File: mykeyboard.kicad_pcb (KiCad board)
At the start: 2 copper layers, 91.4 x 55.9 mm, 23 parts, among them J1 MJ-4PP-9, SW1 SW_PUSH, SW2 SW_PUSH, SW3 SW_PUSH, SW4 SW_PUSH, SW5 SW_PUSH, SW6 SW_PUSH, SW7 SW_PUSH, SW8 SW_PUSH, SW9 SW_PUSH, U1 ProMicro

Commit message: Pro micro の配置と回路の配線
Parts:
- added U1: ProMicro, Keebio-Parts:ArduinoProMicro-BackSide, B.Cu at (137.2, 90.2)
- U1: footprint kbd:ProMicro_v2 -> Keebio-Parts:ArduinoProMicro-BackSide
- moved J1 36.8 mm to (172.7, 75.0)
- moved U1 19.7 mm to (156.2, 90.2)
- moved D1 12.7 mm to (118.1, 104.1), turned to 180 degrees
- moved D5 1.27 mm to (118.1, 108.0)
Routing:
- net row1: track 0.00 -> 113.4 mm
- net col2: track 0.00 -> 95.8 mm
- net col3: track 0.00 -> 93.4 mm
- net row0: track 0.00 -> 87.6 mm
- net GND: track 0.00 -> 71.1 mm
- net col0: track 0.00 -> 58.6 mm
- net VCC: track 0.00 -> 48.7 mm
- net col1: track 0.00 -> 47.4 mm
- net reset: track 0.00 -> 44.7 mm
- net Net-(U1-Pad16): track 0.00 -> 37.1 mm
- net Net-(D2-Pad1): track 0.00 -> 37.1 mm
- net Net-(U1-Pad14): track 0.00 -> 35.3 mm
- net Net-(U1-Pad15): track 0.00 -> 35.3 mm
- net Net-(U1-Pad24): track 0.00 -> 35.3 mm
- net Net-(U1-Pad13): track 0.00 -> 35.3 mm
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
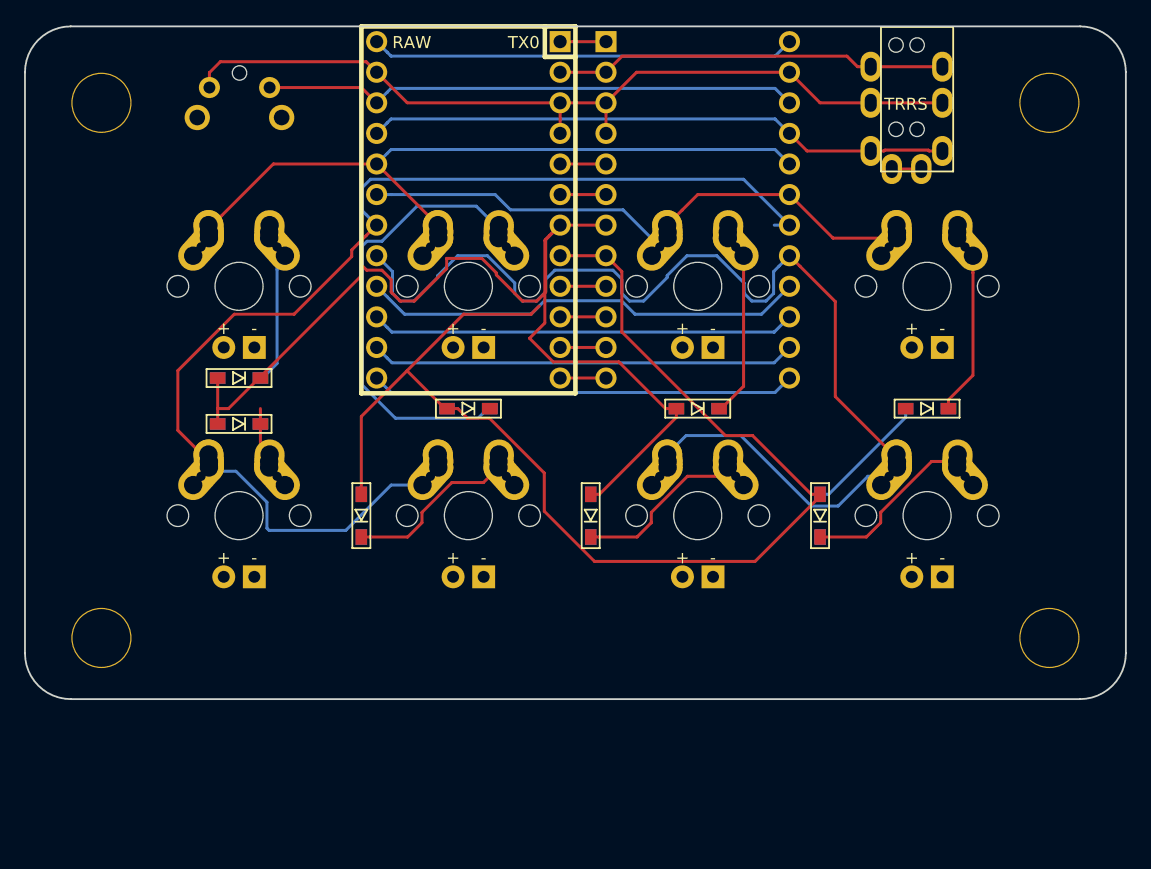
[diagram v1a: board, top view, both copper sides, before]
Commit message: 配線をリセット、ダイオードの位置をまとめた
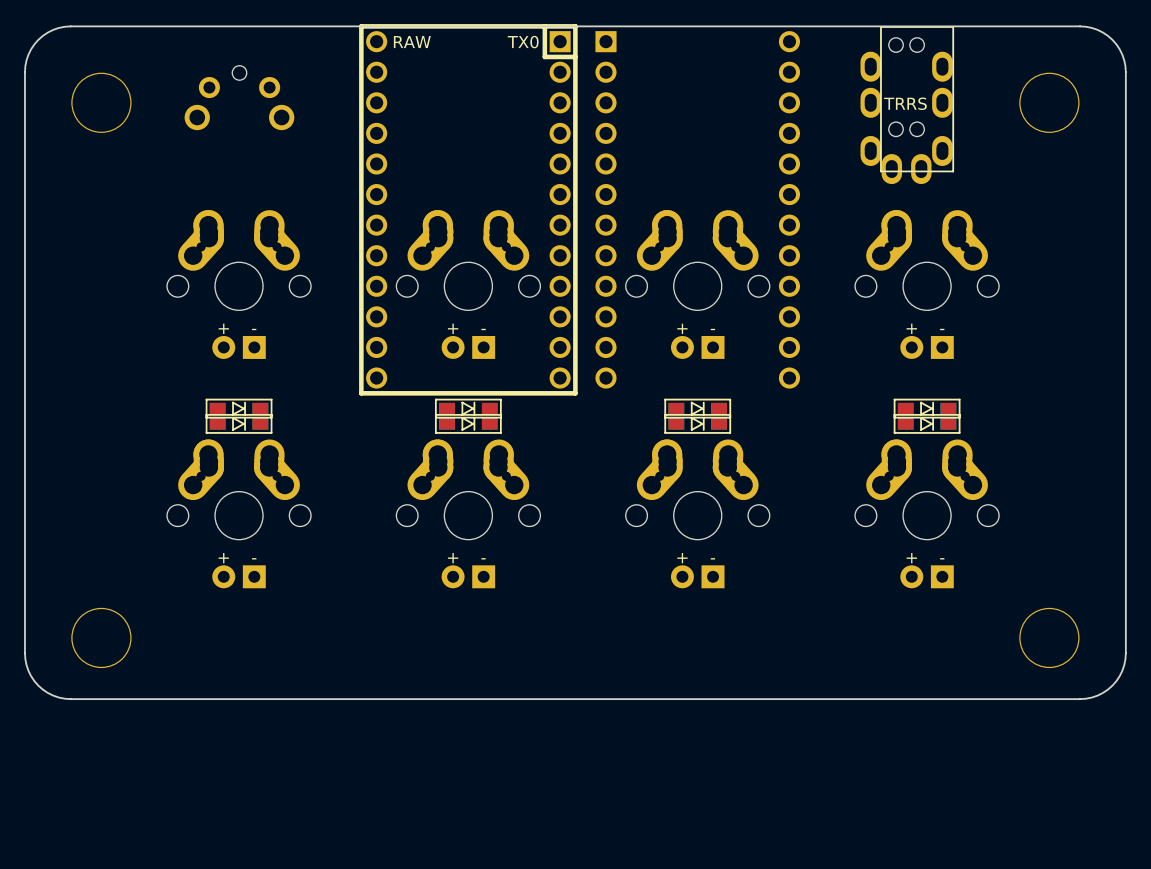
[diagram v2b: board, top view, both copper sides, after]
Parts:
- moved D7 11.7 mm to (156.2, 108.0), turned to 180 degrees
- moved D6 11.7 mm to (137.2, 108.0), turned to 180 degrees
- moved D8 11.7 mm to (175.3, 108.0), turned to 180 degrees
- moved D1 2.54 mm to (118.1, 106.7)
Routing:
- net row1: track 113.4 -> 0.00 mm
- net col2: track 95.8 -> 0.00 mm
- net col3: track 93.4 -> 0.00 mm
- net row0: track 87.6 -> 0.00 mm
- net GND: track 71.1 -> 0.00 mm
- net col0: track 58.6 -> 0.00 mm
- net VCC: track 48.7 -> 0.00 mm
- net col1: track 47.4 -> 0.00 mm
- net reset: track 44.7 -> 0.00 mm
- net Net-(U1-Pad16): track 37.1 -> 0.00 mm
- net Net-(D2-Pad1): track 37.1 -> 0.00 mm
- net Net-(U1-Pad14): track 35.3 -> 0.00 mm
- net Net-(U1-Pad15): track 35.3 -> 0.00 mm
- net Net-(U1-Pad24): track 35.3 -> 0.00 mm
- net Net-(U1-Pad13): track 35.3 -> 0.00 mm
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
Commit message: 回路図の Pro Micro のフットプリントを Keebio の Backside 版に更新、PCB にフットプリントを全て反映
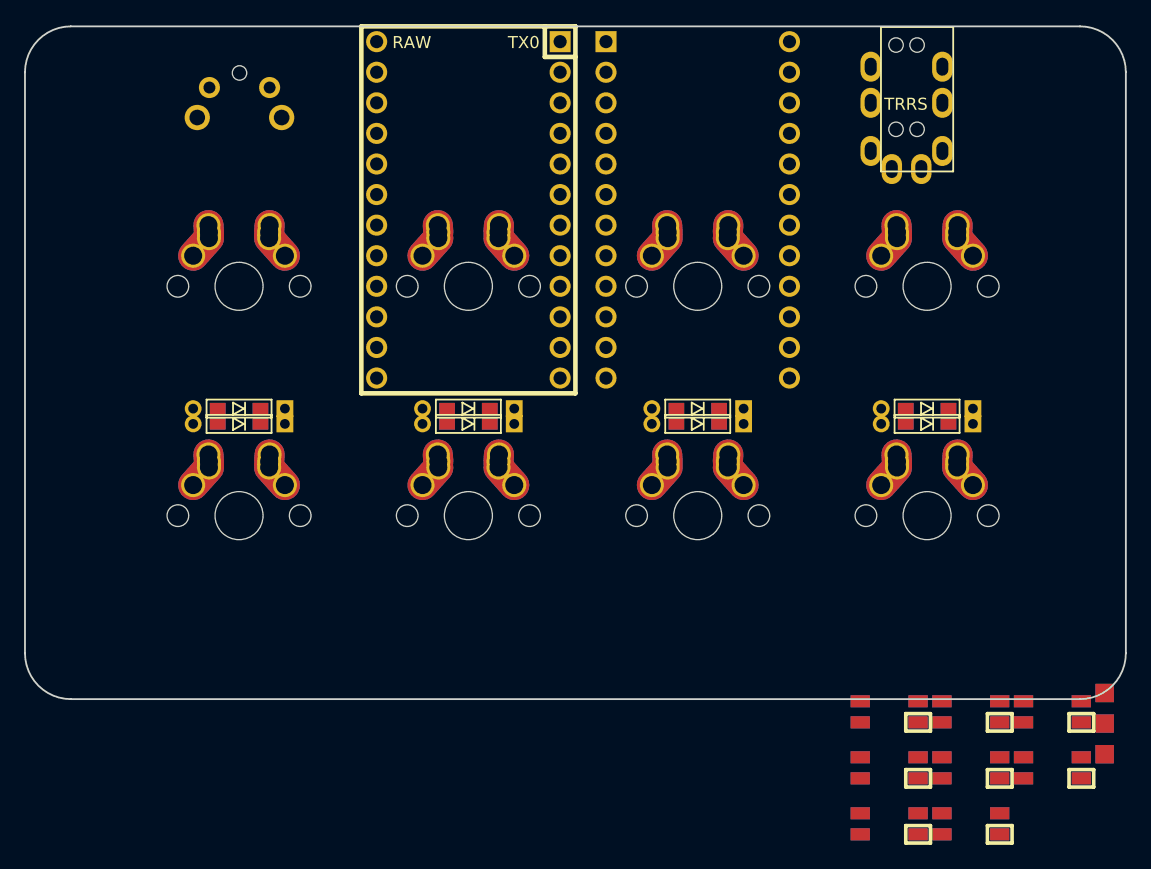
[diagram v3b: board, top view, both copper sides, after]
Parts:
- removed Ref** (x4): Val**, kbd:HOLE
- added J2: LED, kbd:StripLED_rev, F.Cu at (190.0, 130.3)
- added L1: SK6812MINI, kbd:SK6812MINI_rev, F.Cu at (172.1, 131.9)
- added L2: SK6812MINI, kbd:SK6812MINI_rev, F.Cu at (172.1, 136.5)
- added L3: SK6812MINI, kbd:SK6812MINI_rev, F.Cu at (178.9, 131.9)
- added L4: SK6812MINI, kbd:SK6812MINI_rev, F.Cu at (172.1, 141.2)
- added L5: SK6812MINI, kbd:SK6812MINI_rev, F.Cu at (178.9, 136.5)
- added L6: SK6812MINI, kbd:SK6812MINI_rev, F.Cu at (185.7, 131.9)
- added L7: SK6812MINI, kbd:SK6812MINI_rev, F.Cu at (178.9, 141.2)
- added L8: SK6812MINI, kbd:SK6812MINI_rev, F.Cu at (185.7, 136.5)
- D1, D2, D3, D4, D5, D6, D7, D8: footprint kbd:D3_SMD -> kbd:D3_TH_SMD
- SW1, SW2, SW3, SW4, SW5, SW6, SW7, SW8: footprint Keebio-Parts:Hybrid_PCB_100H_Dual_hole-LED -> Keebio-Parts:Hybrid_PCB_100H_Dual_hole
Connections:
- U1 pad 1: Net-(U1-Pad1) -> led

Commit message: LED を配置、ダイオードの位置を変更
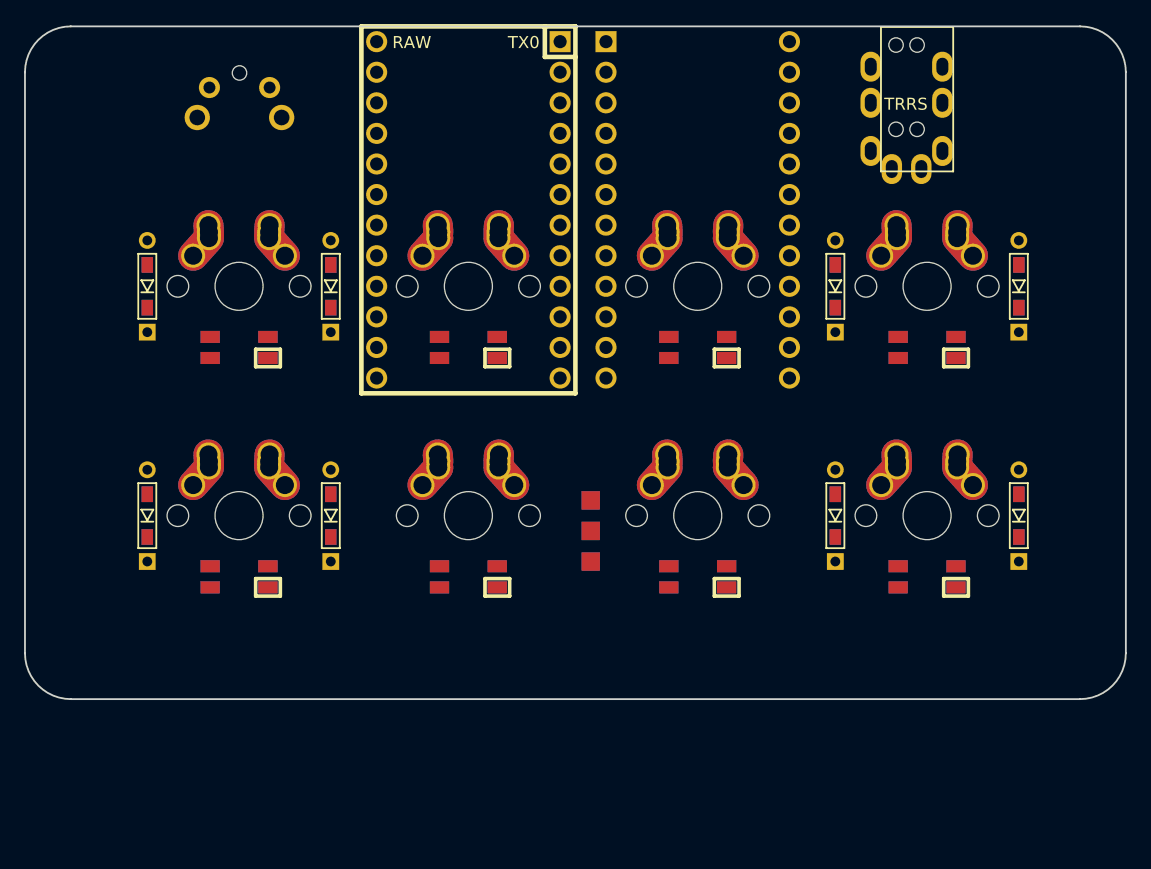
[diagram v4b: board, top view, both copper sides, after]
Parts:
- moved L8 76.0 mm to (118.1, 101.6)
- moved L7 64.1 mm to (118.1, 120.7)
- moved L3 51.5 mm to (137.2, 101.6)
- moved J2 45.6 mm to (147.3, 114.3)
- moved L5 44.6 mm to (137.2, 120.7)
- moved L1 34.2 mm to (156.2, 101.6)
- moved L6 32.0 mm to (175.3, 101.6)
- moved L2 22.5 mm to (156.2, 120.7)
- moved L4 20.8 mm to (175.3, 120.7)
- moved D2 15.3 mm to (125.7, 96.5), turned to 90 degrees
- moved D3 15.3 mm to (167.6, 96.5), turned to 90 degrees
- moved D6 13.7 mm to (125.7, 115.6), turned to 90 degrees
- moved D7 13.7 mm to (167.6, 115.6), turned to 90 degrees
- moved D1 12.7 mm to (110.5, 96.5), turned to 90 degrees
- moved D4 12.7 mm to (182.9, 96.5), turned to 90 degrees
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
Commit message: 裏面 Pro Mirco が接続されていなかったので修正
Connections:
- U1 pad 1: Net-(U1-Pad1) -> led

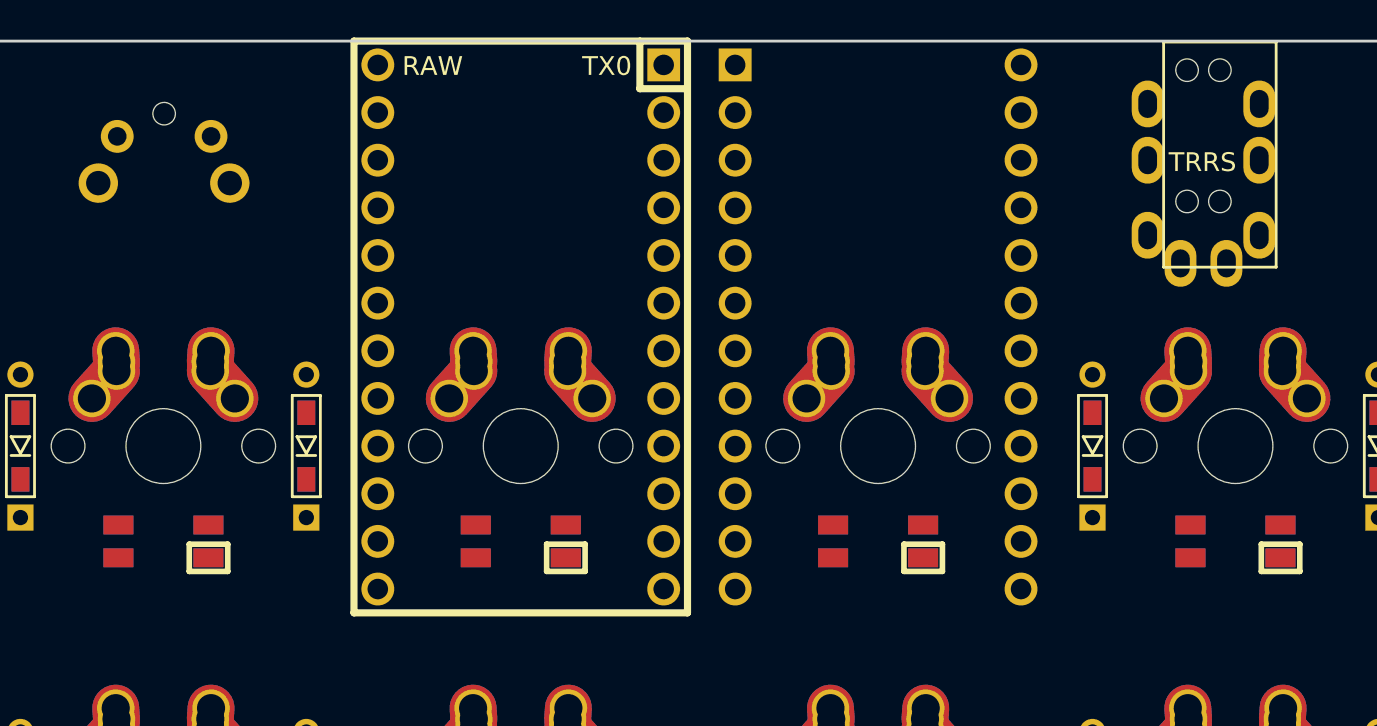
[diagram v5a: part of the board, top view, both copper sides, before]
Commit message: 配置の順番がおかしくなっていたのを修正、Pro Micro を配線
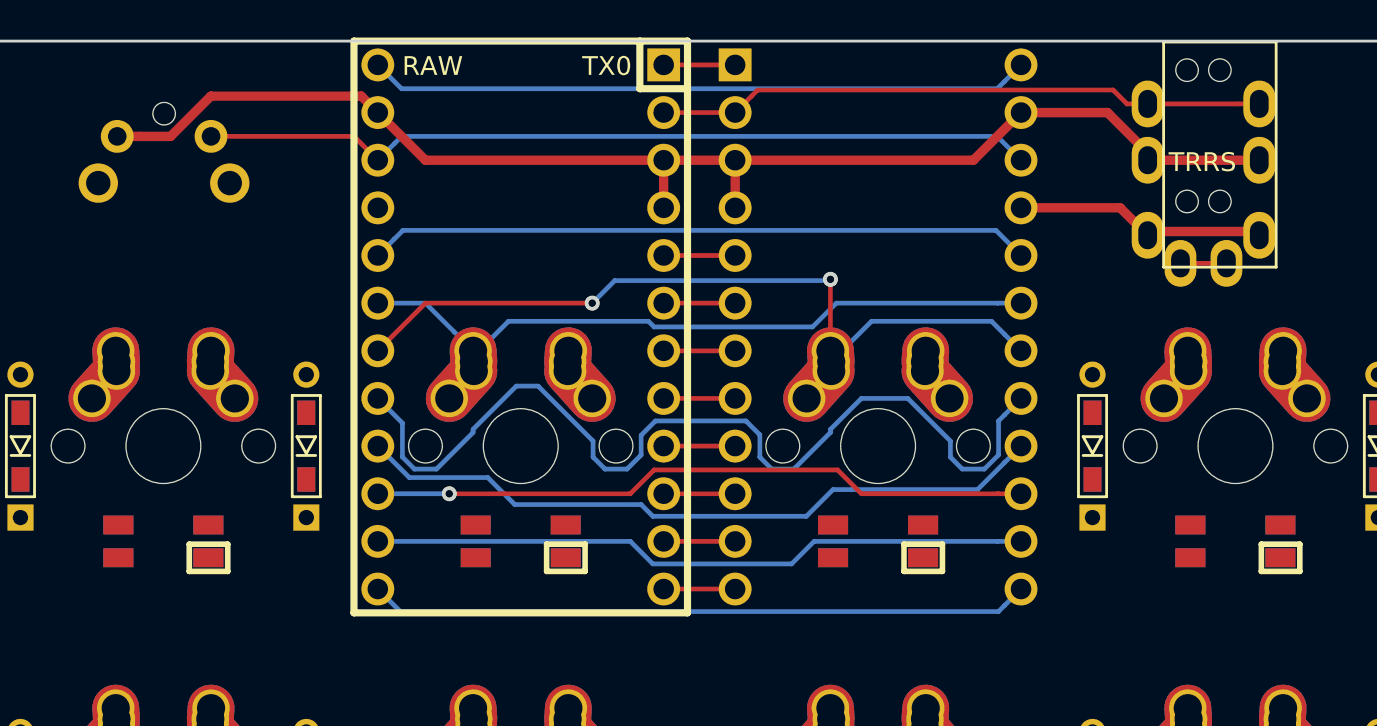
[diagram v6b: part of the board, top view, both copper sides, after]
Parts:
- moved D4 60.2 mm to (125.7, 115.6)
- moved L7 60.2 mm to (175.3, 101.6)
- moved L8 60.2 mm to (175.3, 120.7)
- moved SW5 42.6 mm to (156.2, 96.5)
- moved SW4 42.6 mm to (137.2, 115.6)
- moved D6 41.9 mm to (167.6, 115.6)
- moved L1 38.1 mm to (118.1, 101.6)
- moved L2 38.1 mm to (118.1, 120.7)
- moved L4 38.1 mm to (137.2, 120.7)
- moved L5 26.9 mm to (156.2, 101.6)
- moved L6 26.9 mm to (156.2, 120.7)
- moved SW2 26.9 mm to (118.1, 115.6)
- moved SW7 26.9 mm to (175.3, 96.5)
- moved D2 24.4 mm to (110.5, 115.6)
- moved D5 24.4 mm to (125.7, 96.5)
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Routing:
- net GND: track 0.00 -> 70.6 mm
- net col3: track 0.00 -> 51.0 mm
- net reset: track 0.00 -> 44.8 mm
- net col2: track 0.00 -> 41.2 mm, vias 0 -> 2
- net Net-(U1-Pad16): track 0.00 -> 37.4 mm
- net col1: track 0.00 -> 36.7 mm
- net col0: track 0.00 -> 35.4 mm
- net Net-(U1-Pad24): track 0.00 -> 35.3 mm
- net Net-(U1-Pad15): track 0.00 -> 35.3 mm, vias 0 -> 1
- net Net-(U1-Pad14): track 0.00 -> 35.3 mm
- net Net-(U1-Pad13): track 0.00 -> 35.3 mm
- net data: track 0.00 -> 32.6 mm
- net VCC: track 0.00 -> 13.5 mm
- net row1: track 0.00 -> 3.81 mm
- net row0: track 0.00 -> 3.81 mm
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
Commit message: 配線を済ませた
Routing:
- net VCC: track 13.5 -> 277.0 mm, vias 0 -> 12
- net GND: track 70.6 -> 297.2 mm, vias 0 -> 18
- net row1: track 3.81 -> 115.2 mm, vias 0 -> 5
- net row0: track 3.81 -> 101.0 mm, vias 0 -> 2
- net led: track 3.81 -> 92.4 mm, vias 0 -> 3
- net Net-(L4-Pad1): track 0.00 -> 56.7 mm, vias 0 -> 4
- net Net-(D5-Pad1): track 0.00 -> 49.7 mm
- net Net-(L2-Pad1): track 0.00 -> 45.6 mm, vias 0 -> 4
- net col0: track 35.4 -> 79.3 mm, vias 0 -> 1
- net Net-(D3-Pad1): track 0.00 -> 43.8 mm, vias 0 -> 1
- net Net-(L1-Pad1): track 0.00 -> 39.8 mm, vias 0 -> 2
- net Net-(L6-Pad1): track 0.00 -> 37.1 mm, vias 0 -> 4
- net Net-(L3-Pad3): track 0.00 -> 32.6 mm, vias 0 -> 2
- net col1: track 36.7 -> 69.2 mm, vias 0 -> 1
- net col2: track 41.2 -> 69.0 mm, vias 2 -> 5
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
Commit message: 余計なビアを削除
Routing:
- net row1: vias 5 -> 4
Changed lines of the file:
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@@
     (thickness 1.6)
     (drawings 8)
-    (tracks 726)
+    (tracks 725)
     (zones 0)
     (modules 29)
@@
   (segment (start 110.49 111.76) (end 110.49 113.795) (width 0.25) (layer F.Cu) (net 4))
   (segment (start 125.73 111.76) (end 130.613002 111.76) (width 0.25) (layer B.Cu) (net 4))
-  (via (at 144.78 93.98) (size 0.8) (drill 0.4) (layers F.Cu B.Cu) (net 4))
   (via (at 146.05 111.76) (size 0.8) (drill 0.4) (layers F.Cu B.Cu) (net 4))
   (via (at 148.59 111.76) (size 0.8) (drill 0.4) (layers F.Cu B.Cu) (net 4))
